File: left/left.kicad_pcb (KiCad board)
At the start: 2 copper layers, 158.5 x 116.8 mm, 57 parts, among them J1 MJ-4PP-9, U1 ProMicro

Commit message: 左手PCB完成
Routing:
- net col6: track 0.00 -> 333.7 mm, vias 0 -> 2
- net col7: track 0.00 -> 296.9 mm, vias 0 -> 2
- net col5: track 0.00 -> 295.4 mm, vias 0 -> 2
- net col4: track 0.00 -> 285.7 mm, vias 0 -> 3
- net col3: track 0.00 -> 262.3 mm, vias 0 -> 2
- net col2: track 0.00 -> 246.2 mm, vias 0 -> 2
- net GND: track 0.00 -> 243.8 mm, vias 0 -> 3
- net row1: track 0.00 -> 223.7 mm
- net pwr: track 0.00 -> 221.7 mm
- net data: track 0.00 -> 191.8 mm, vias 0 -> 1
- net row3: track 0.00 -> 180.1 mm
- net row2: track 0.00 -> 175.6 mm, vias 0 -> 2
- net col1: track 0.00 -> 165.3 mm, vias 0 -> 1
- net row4: track 0.00 -> 160.7 mm
- net Net-(D6-A): track 0.00 -> 54.3 mm
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- added copper zone on B.Cu, net GND
- added copper zone on F.Cu, net GND

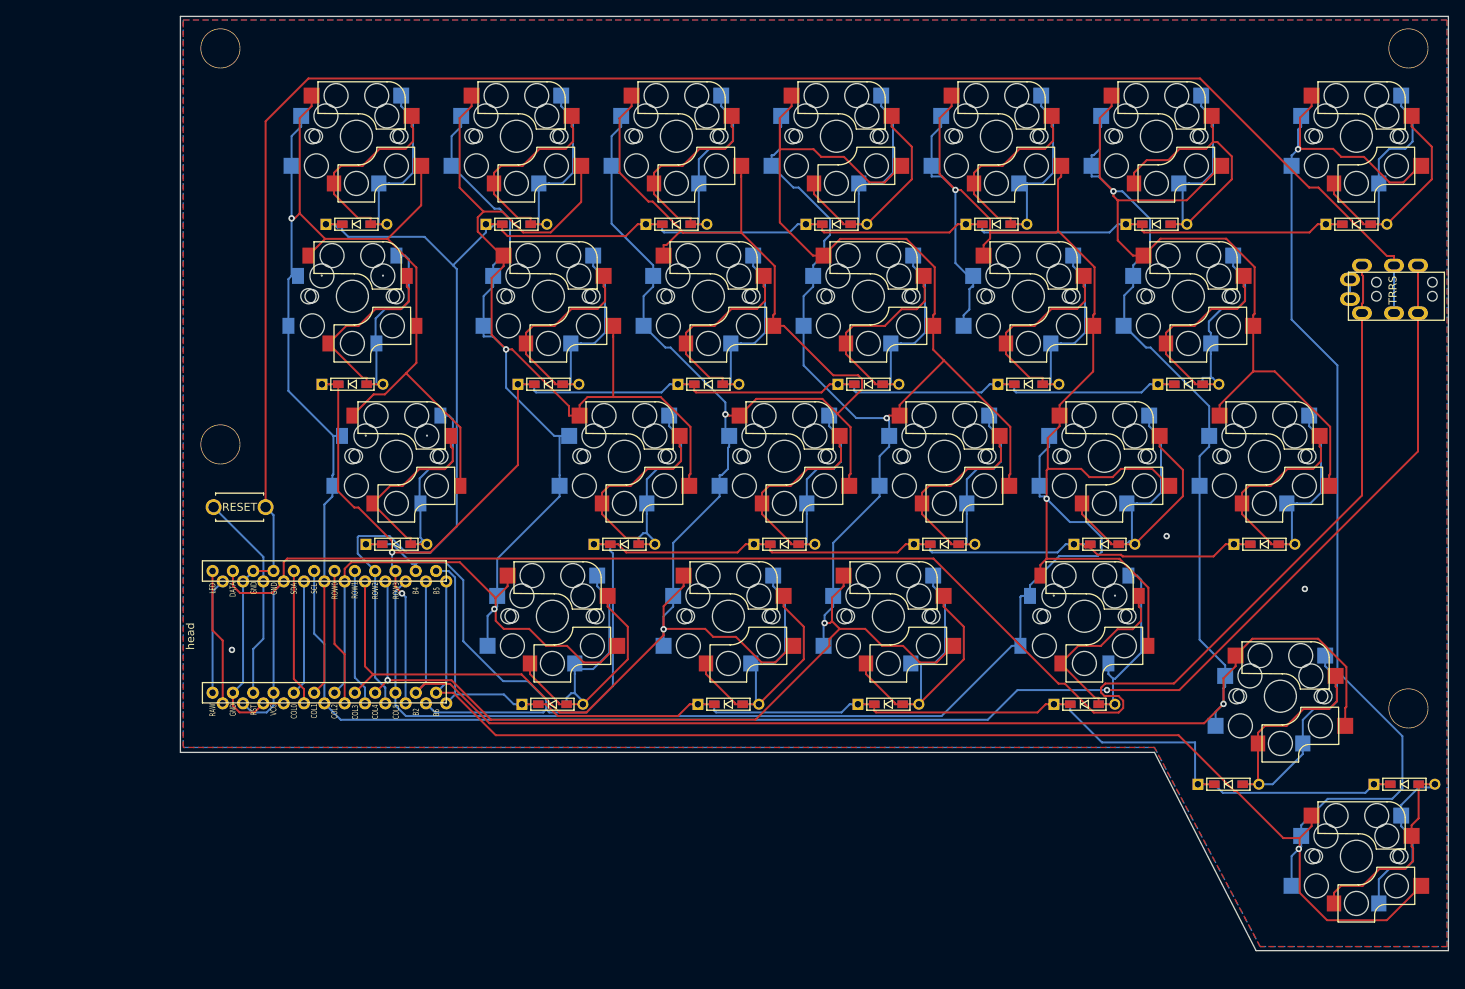
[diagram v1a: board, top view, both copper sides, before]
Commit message: 左手PCBの組み換え．外枠は未完成
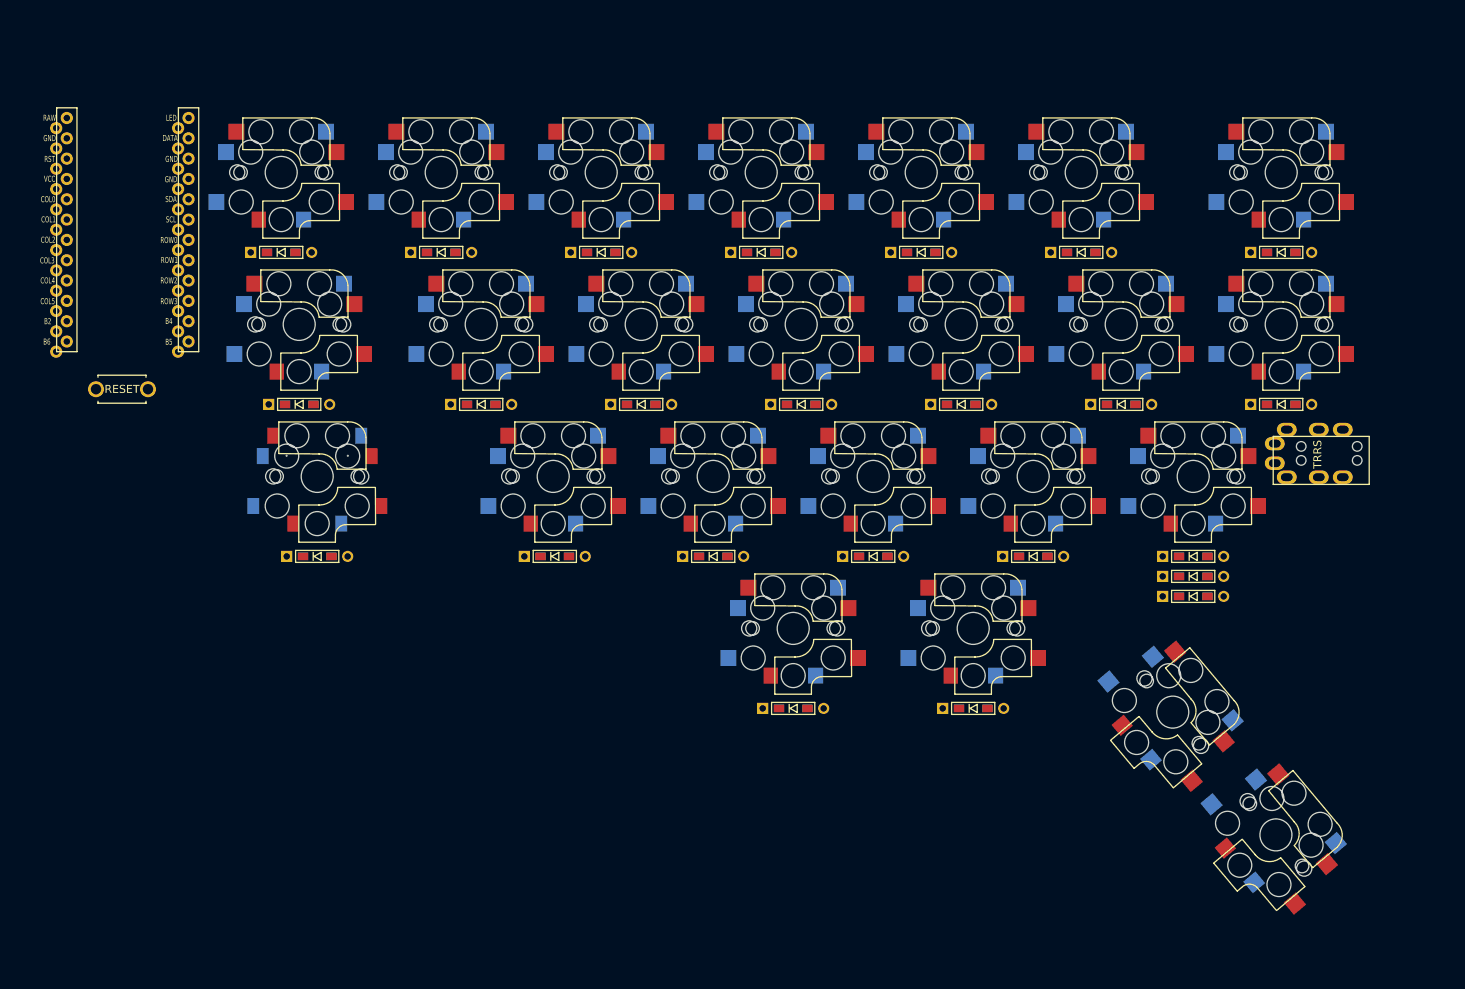
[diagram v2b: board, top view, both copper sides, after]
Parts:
- removed D25: D, kbd:D3_TH_SMD
- removed LEFT_SW25: SW_PUSH, kbd:CherryMX_Choc_Hotswap
- removed Ref**: Val**, kbd:HOLE
- removed Ref01: Val01, kbd:HOLE
- removed Ref02: Val02, kbd:HOLE
- removed Ref03: Val03, kbd:HOLE
- LEFT_SW13, LEFT_SW22, LEFT_SW7: footprint kbd:CherryMX_Choc_Hotswap_1.5u -> kbd:CherryMX_Choc_Hotswap
- LEFT_SW15: footprint kbd:CherryMX_Choc_Hotswap -> kbd:CherryMX_Choc_Hotswap_1.5u
- moved D7 117.3 mm to (191.1, 57.5)
- moved LEFT_SW7 117.1 mm to (191.1, 47.5), turned to 0 degrees
- moved D13 92.3 mm to (171.1, 76.5)
- moved LEFT_SW13 92.1 mm to (171.1, 66.5), turned to 0 degrees
- moved LEFT_SW24 87.9 mm to (190.4, 130.3), turned to -50 degrees
- moved D14 83.9 mm to (191.1, 76.5)
- moved LEFT_SW14 83.7 mm to (191.1, 66.5)
- moved D19 62.9 mm to (160.1, 95.5)
- moved LEFT_SW19 62.6 mm to (160.1, 85.5)
- moved D20 61.0 mm to (180.1, 95.5)
- moved LEFT_SW20 60.7 mm to (180.1, 85.5)
- moved LEFT_SW15 58.5 mm to (70.6, 85.5), turned to -90 degrees
- moved D15 58.4 mm to (70.6, 95.5)
- moved U1 55.8 mm to (46.9, 55.2), turned to 0 degrees
- moved D24 50.8 mm to (180.1, 100.5)
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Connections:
- D13 pad 1: row3 -> row2
- D14 pad 1: row3 -> row2
- D19 pad 1: row4 -> row3
- D20 pad 1: row4 -> row3
- D24 pad 1: row1 -> row4
- D7 pad 1: row2 -> row1
- LEFT_SW10 pad 1: col4 -> col3
- LEFT_SW11 pad 1: col5 -> col4
- LEFT_SW12 pad 1: col6 -> col5
- LEFT_SW13 pad 1: col1 -> col6
- LEFT_SW14 pad 1: col2 -> col7
- LEFT_SW15 pad 1: col3 -> col1
- LEFT_SW16 pad 1: col4 -> col2
- LEFT_SW17 pad 1: col5 -> col3
- LEFT_SW18 pad 1: col6 -> col4
- LEFT_SW19 pad 1: col2 -> col5
- LEFT_SW20 pad 1: col3 -> col6
- LEFT_SW7 pad 1: col1 -> col7
- LEFT_SW8 pad 1: col2 -> col1
- LEFT_SW9 pad 1: col3 -> col2
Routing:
- net col6: track 333.7 -> 0.00 mm, vias 2 -> 0
- net col7: track 296.9 -> 0.00 mm, vias 2 -> 0
- net col5: track 295.4 -> 0.00 mm, vias 2 -> 0
- net col4: track 285.7 -> 0.00 mm, vias 3 -> 0
- net col3: track 262.3 -> 0.00 mm, vias 2 -> 0
- net col2: track 246.2 -> 0.00 mm, vias 2 -> 0
- net GND: track 243.8 -> 0.00 mm, vias 3 -> 0
- net row1: track 223.7 -> 0.00 mm
- net pwr: track 221.7 -> 0.00 mm
- net data: track 191.8 -> 0.00 mm, vias 1 -> 0
- net row3: track 180.1 -> 0.00 mm
- net row2: track 175.6 -> 0.00 mm, vias 2 -> 0
- net col1: track 165.3 -> 0.00 mm, vias 1 -> 0
- net row4: track 160.7 -> 0.00 mm
- net Net-(D6-A): track 54.3 -> 0.00 mm
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- removed copper zone on B.Cu, net GND
- removed copper zone on F.Cu, net GND
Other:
- board outline removed

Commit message: 左手PCB完成
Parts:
- added Ref01: Val01, kbd:HOLE, F.Cu at (40.4, 74.8)
- added Ref02: Val02, kbd:HOLE, F.Cu at (178.6, 40.6)
- added Ref03: Val03, kbd:HOLE, F.Cu at (168.6, 101.6)
- moved LEFT_SW_RESET1 4.12 mm to (50.3, 75.0)
- moved U1 1.44 mm to (46.8, 53.7)
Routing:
- net col6: track 0.00 -> 403.2 mm, vias 0 -> 2
- net col5: track 0.00 -> 392.6 mm, vias 0 -> 1
- net col7: track 0.00 -> 380.7 mm, vias 0 -> 3
- net col4: track 0.00 -> 326.7 mm, vias 0 -> 1
- net col3: track 0.00 -> 218.7 mm, vias 0 -> 3
- net data: track 0.00 -> 217.3 mm, vias 0 -> 2
- net pwr: track 0.00 -> 205.5 mm, vias 0 -> 1
- net col2: track 0.00 -> 201.3 mm, vias 0 -> 2
- net row4: track 0.00 -> 198.3 mm
- net row3: track 0.00 -> 184.7 mm
- net row2: track 0.00 -> 182.1 mm
- net row1: track 0.00 -> 174.9 mm, vias 0 -> 2
- net col1: track 0.00 -> 163.0 mm, vias 0 -> 2
- net Net-(D23-A): track 0.00 -> 83.0 mm
- net Net-(D24-A): track 0.00 -> 72.4 mm, vias 0 -> 1
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- added copper zone on B.Cu, net GND
- added copper zone on F.Cu, net GND
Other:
- board outline added: 174.9 x 112.3 mm
